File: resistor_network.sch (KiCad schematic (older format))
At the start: 0 parts

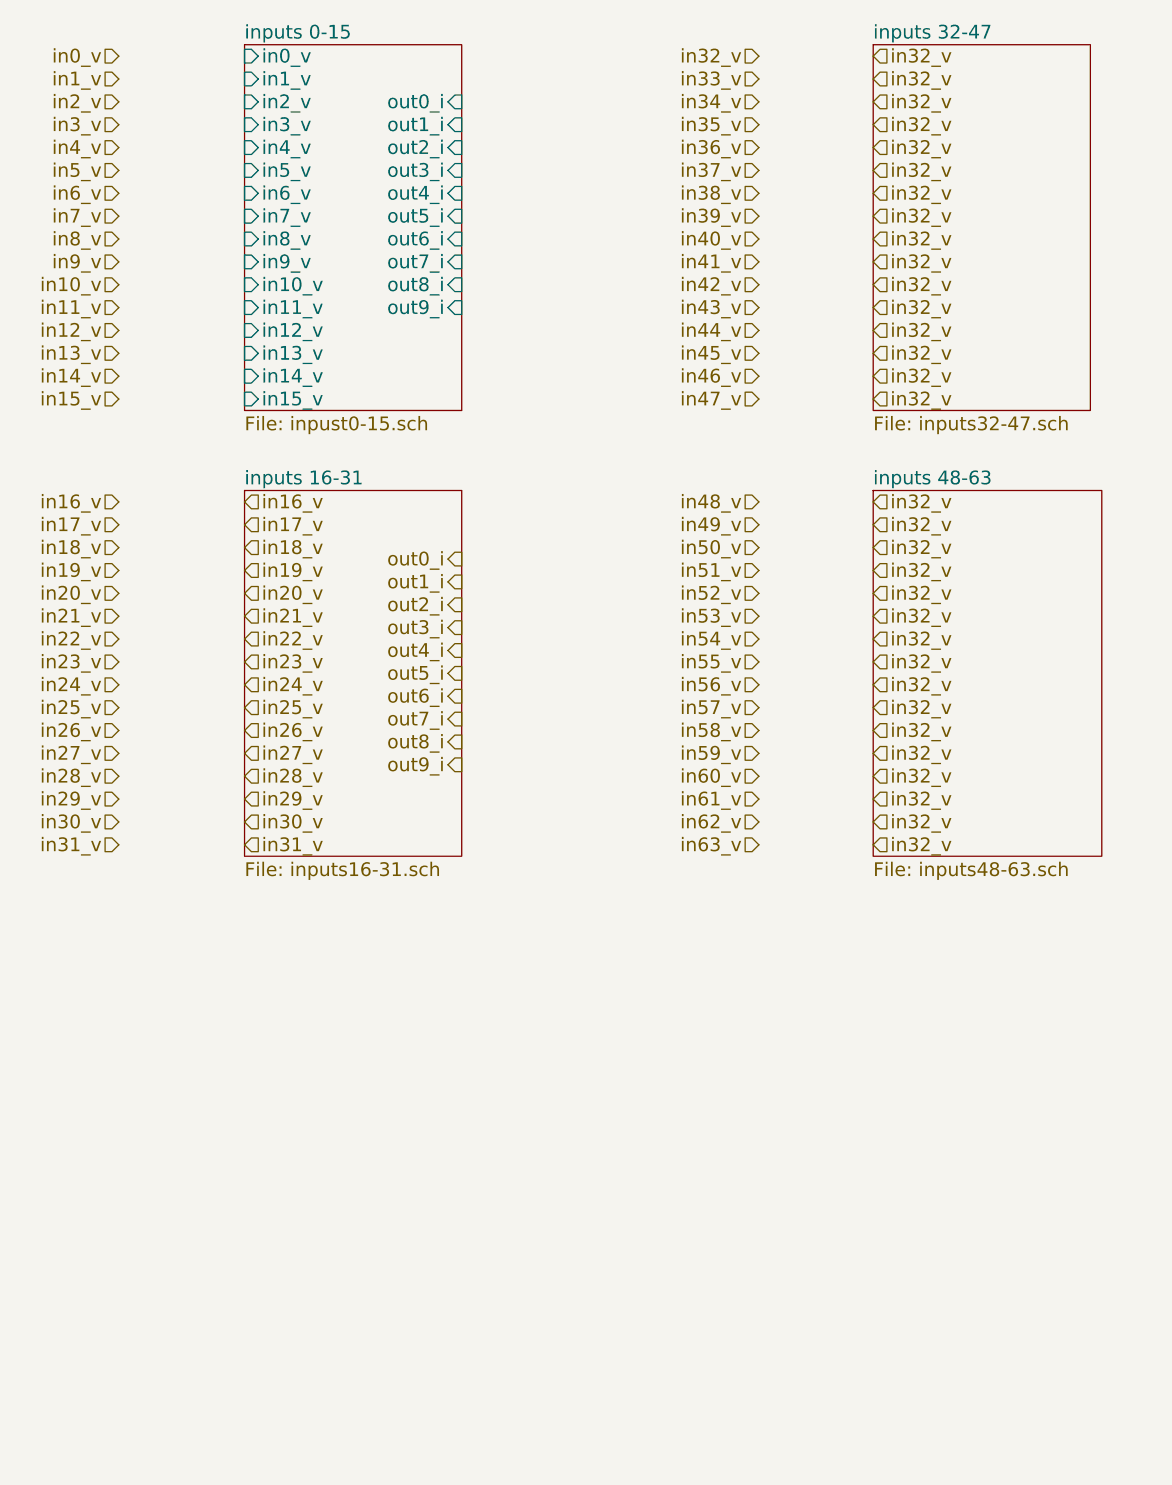
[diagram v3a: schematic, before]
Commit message: added wires from input to output
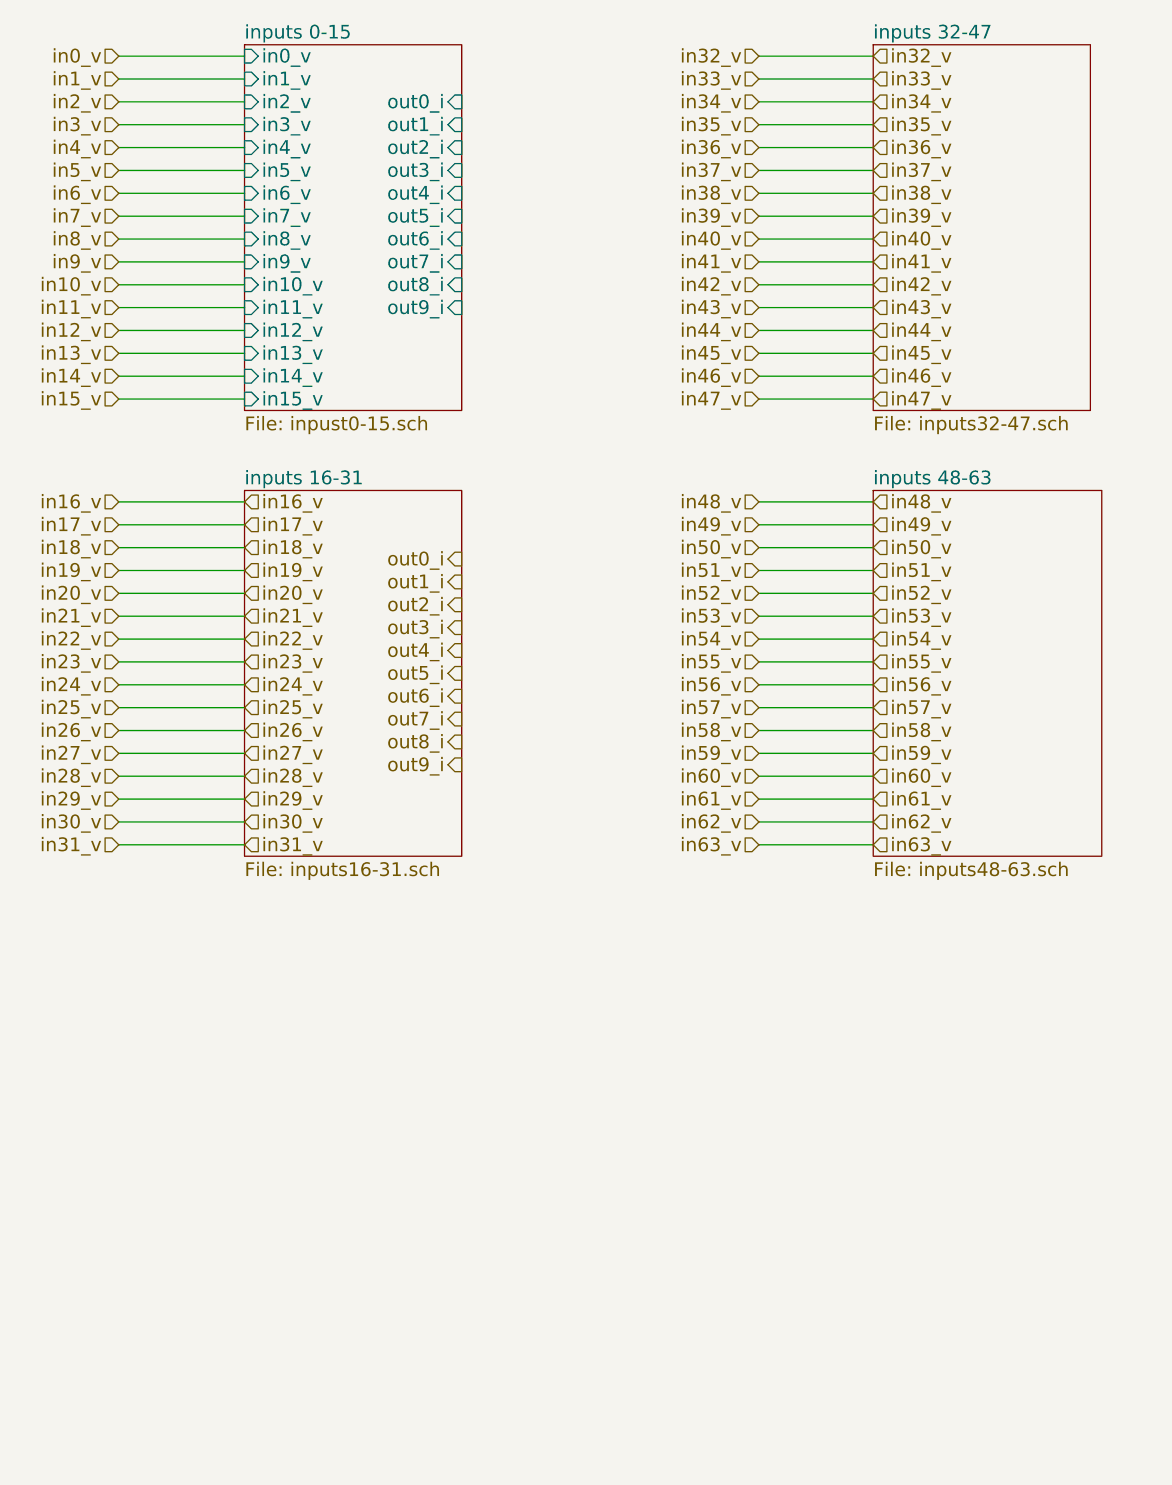
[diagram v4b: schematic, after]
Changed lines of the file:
@@
 in32_v
 Text HLabel 4950 1200 2    60   Input ~ 0
-in32_v
+in33_v
 Text HLabel 4950 1300 2    60   Input ~ 0
-in32_v
+in34_v
 Text HLabel 4950 1400 2    60   Input ~ 0
-in32_v
+in35_v
 Text HLabel 4950 1500 2    60   Input ~ 0
-in32_v
+in36_v
 Text HLabel 4950 1600 2    60   Input ~ 0
-in32_v
+in37_v
 Text HLabel 4950 1700 2    60   Input ~ 0
-in32_v
+in38_v
 Text HLabel 4950 1800 2    60   Input ~ 0
-in32_v
+in39_v
 Text HLabel 4950 1900 2    60   Input ~ 0
-in32_v
+in40_v
 Text HLabel 4950 2000 2    60   Input ~ 0
-in32_v
+in41_v
 Text HLabel 4950 2100 2    60   Input ~ 0
-in32_v
+in42_v
 Text HLabel 4950 2200 2    60   Input ~ 0
-in32_v
+in43_v
 Text HLabel 4950 2300 2    60   Input ~ 0
-in32_v
+in44_v
 Text HLabel 4950 2400 2    60   Input ~ 0
-in32_v
+in45_v
 Text HLabel 4950 2500 2    60   Input ~ 0
-in32_v
+in46_v
 Text HLabel 4950 2600 2    60   Input ~ 0
-in32_v
+in47_v
 Text HLabel 4950 3050 2    60   Input ~ 0
-in32_v
+in48_v
 Text HLabel 4950 3150 2    60   Input ~ 0
-in32_v
+in49_v
 Text HLabel 4950 3250 2    60   Input ~ 0
-in32_v
+in50_v
 Text HLabel 4950 3350 2    60   Input ~ 0
-in32_v
+in51_v
 Text HLabel 4950 3450 2    60   Input ~ 0
-in32_v
+in52_v
 Text HLabel 4950 3550 2    60   Input ~ 0
-in32_v
+in53_v
 Text HLabel 4950 3650 2    60   Input ~ 0
-in32_v
+in54_v
 Text HLabel 4950 3750 2    60   Input ~ 0
-in32_v
+in55_v
 Text HLabel 4950 3850 2    60   Input ~ 0
-in32_v
+in56_v
 Text HLabel 4950 3950 2    60   Input ~ 0
-in32_v
+in57_v
 Text HLabel 4950 4050 2    60   Input ~ 0
-in32_v
+in58_v
 Text HLabel 4950 4150 2    60   Input ~ 0
-in32_v
+in59_v
 Text HLabel 4950 4250 2    60   Input ~ 0
-in32_v
+in60_v
 Text HLabel 4950 4350 2    60   Input ~ 0
-in32_v
+in61_v
 Text HLabel 4950 4450 2    60   Input ~ 0
-in32_v
+in62_v
 Text HLabel 4950 4550 2    60   Input ~ 0
-in32_v
+in63_v
+Wire Wire Line
+	1650 1100 2200 1100
+Wire Wire Line
+	1650 1200 2200 1200
+Wire Wire Line
+	1650 1300 2200 1300
+Wire Wire Line
+	1650 1400 2200 1400
+Wire Wire Line
+	1650 1500 2200 1500
+Wire Wire Line
+	1650 1600 2200 1600
+Wire Wire Line
+	1650 1700 2200 1700
+Wire Wire Line
+	1650 1800 2200 1800
+Wire Wire Line
+	1650 1900 2200 1900
+Wire Wire Line
+	1650 2000 2200 2000
+Wire Wire Line
+	1650 2100 2200 2100
+Wire Wire Line
+	1650 2200 2200 2200
+Wire Wire Line
+	1650 2300 2200 2300
+Wire Wire Line
+	1650 2400 2200 2400
+Wire Wire Line
+	1650 2500 2200 2500
+Wire Wire Line
+	1650 2600 2200 2600
+Wire Wire Line
+	1650 3050 2200 3050
+Wire Wire Line
+	1650 3150 2200 3150
+Wire Wire Line
+	1650 3250 2200 3250
+Wire Wire Line
+	1650 3350 2200 3350
+Wire Wire Line
+	1650 3450 2200 3450
+Wire Wire Line
+	1650 3550 2200 3550
+Wire Wire Line
+	1650 3650 2200 3650
+Wire Wire Line
+	1650 3750 2200 3750
+Wire Wire Line
+	1650 3850 2200 3850
+Wire Wire Line
+	1650 3950 2200 3950
+Wire Wire Line
+	1650 4050 2200 4050
+Wire Wire Line
+	1650 4150 2200 4150
+Wire Wire Line
+	1650 4250 2200 4250
+Wire Wire Line
+	1650 4350 2200 4350
+Wire Wire Line
+	1650 4450 2200 4450
+Wire Wire Line
+	1650 4550 2200 4550
+Wire Wire Line
+	4450 1100 4950 1100
+Wire Wire Line
+	4450 1200 4950 1200
+Wire Wire Line
+	4450 1300 4950 1300
+Wire Wire Line
+	4450 1400 4950 1400
+Wire Wire Line
+	4450 1500 4950 1500
+Wire Wire Line
+	4450 1600 4950 1600
+Wire Wire Line
+	4450 1700 4950 1700
+Wire Wire Line
+	4450 1800 4950 1800
+Wire Wire Line
+	4450 1900 4950 1900
+Wire Wire Line
+	4450 2000 4950 2000
+Wire Wire Line
+	4450 2100 4950 2100
+Wire Wire Line
+	4450 2200 4950 2200
+Wire Wire Line
+	4450 2300 4950 2300
+Wire Wire Line
+	4450 2400 4950 2400
+Wire Wire Line
+	4450 2500 4950 2500
+Wire Wire Line
+	4450 2600 4950 2600
+Wire Wire Line
+	4450 3050 4950 3050
+Wire Wire Line
+	4450 3150 4950 3150
+Wire Wire Line
+	4450 3250 4950 3250
+Wire Wire Line
+	4450 3350 4950 3350
+Wire Wire Line
+	4450 3450 4950 3450
+Wire Wire Line
+	4450 3550 4950 3550
+Wire Wire Line
+	4450 3650 4950 3650
+Wire Wire Line
+	4450 3750 4950 3750
+Wire Wire Line
+	4450 3850 4950 3850
+Wire Wire Line
+	4450 3950 4950 3950
+Wire Wire Line
+	4450 4050 4950 4050
+Wire Wire Line
+	4450 4150 4950 4150
+Wire Wire Line
+	4450 4250 4950 4250
+Wire Wire Line
+	4450 4350 4950 4350
+Wire Wire Line
+	4450 4450 4950 4450
+Wire Wire Line
+	4450 4550 4950 4550
 $EndSCHEMATC
